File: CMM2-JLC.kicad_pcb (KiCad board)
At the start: 4 copper layers, 130 x 102 mm, 100 parts, among them J1 Nunchuck, J2 VGA, J3 EXTERNAL I/O, J4 USB_C_Receptacle_USB2.0, J5 Audio, J6 USB A Host, J7 SWD, J8 Micro_SD_Card_Det, J9 Boot select, SW1 Reset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

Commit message: VGA DAC gelayoutet
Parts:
- moved C1 329.2 mm to (-74.8, 78.2)
- moved C13 329.2 mm to (-74.8, 76.2)
- moved C14 329.2 mm to (-61.1, 63.9)
- moved C15 329.2 mm to (-95.2, 95.3)
- moved C2 329.2 mm to (-92.3, 94.8)
- moved C4 329.2 mm to (-82.1, 82.5)
- moved C5 329.2 mm to (-102.4, 104.1)
- moved C6 329.2 mm to (-93.6, 83.0)
- moved C7 329.2 mm to (-71.5, 64.2)
- moved C8 329.2 mm to (-83.2, 85.0)
- moved R1 329.2 mm to (-77.8, 78.2)
- moved R3 329.2 mm to (-79.2, 80.2)
- moved R42 329.2 mm to (-86.1, 87.0)
- moved R43 329.2 mm to (-72.0, 68.9)
- moved R46 329.2 mm to (-92.7, 92.8)
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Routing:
- net /RESET: track 0.00 -> 56.4 mm
- net /VGA_RED: track 0.00 -> 9.84 mm
- net /PH1: track 0.00 -> 9.28 mm
- net /PH0: track 0.00 -> 9.24 mm
- net /VGA_BLUE: track 0.00 -> 8.17 mm
- net /PC15: track 0.00 -> 8.03 mm
- net /VGA_GREEN: track 0.00 -> 8.01 mm
- net /PC14: track 0.00 -> 7.94 mm
- net Net-(R32-Pad1): track 0.00 -> 3.04 mm
- net Net-(R25-Pad1): track 0.00 -> 3.02 mm
- net Net-(R13-Pad2): track 0.00 -> 3.02 mm
- net Net-(R26-Pad1): track 0.00 -> 3.02 mm
- net Net-(R20-Pad1): track 0.00 -> 3.02 mm
- net Net-(R19-Pad1): track 0.00 -> 3.02 mm
- net Net-(R14-Pad1): track 0.00 -> 3.02 mm
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
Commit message: VGA Routing
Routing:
- net /PI10: track 0.00 -> 96.6 mm, vias 0 -> 2
- net /PI9: track 0.00 -> 93.0 mm, vias 0 -> 2
- net /PC0: track 0.00 -> 82.2 mm, vias 0 -> 4
- net /PB1: track 0.00 -> 77.7 mm, vias 0 -> 4
- net /PI4: track 0.00 -> 75.8 mm
- net /PG10: track 0.00 -> 75.2 mm, vias 0 -> 2
- net /PI5: track 0.00 -> 72.7 mm
- net /PG11: track 0.00 -> 69.8 mm
- net /PI6: track 0.00 -> 69.6 mm
- net /PI7: track 0.00 -> 68.0 mm
- net /PH10: track 0.00 -> 60.9 mm, vias 0 -> 4
- net /PH9: track 0.00 -> 58.5 mm, vias 0 -> 4
- net /PG6: track 0.00 -> 58.2 mm, vias 0 -> 2
- net /PI2: track 0.00 -> 50.4 mm, vias 0 -> 2
- net /PH13: track 0.00 -> 44.7 mm, vias 0 -> 2
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
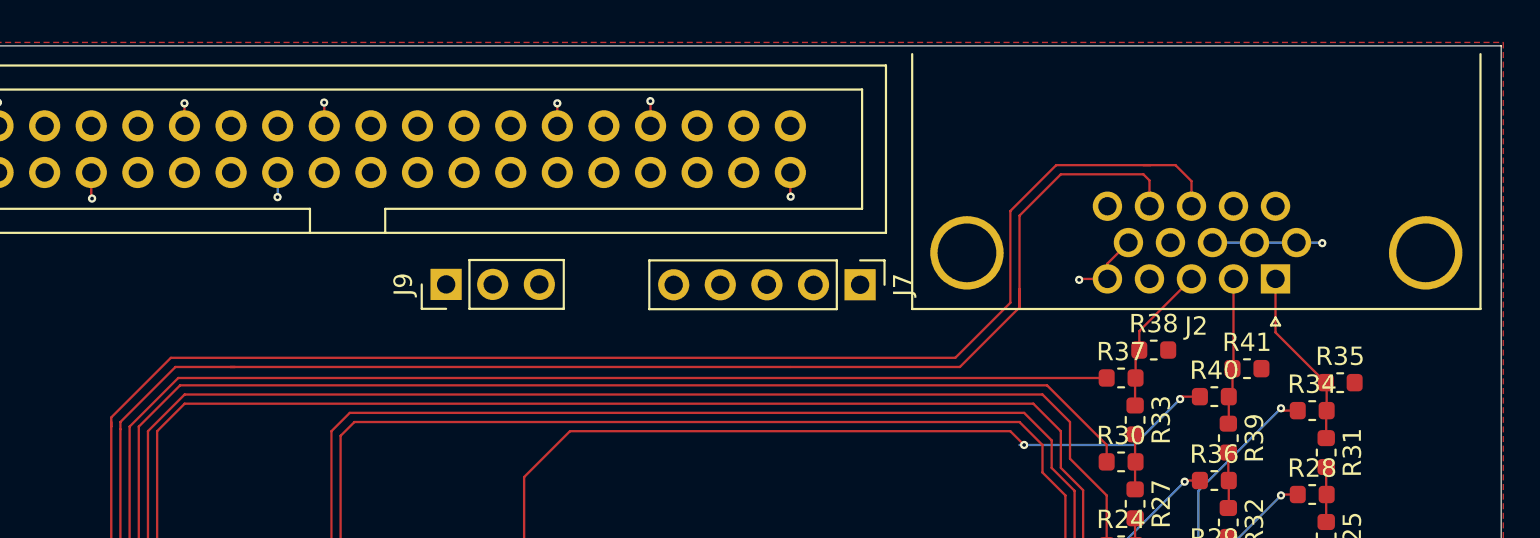
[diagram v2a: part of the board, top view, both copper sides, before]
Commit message: Replace VGA connector
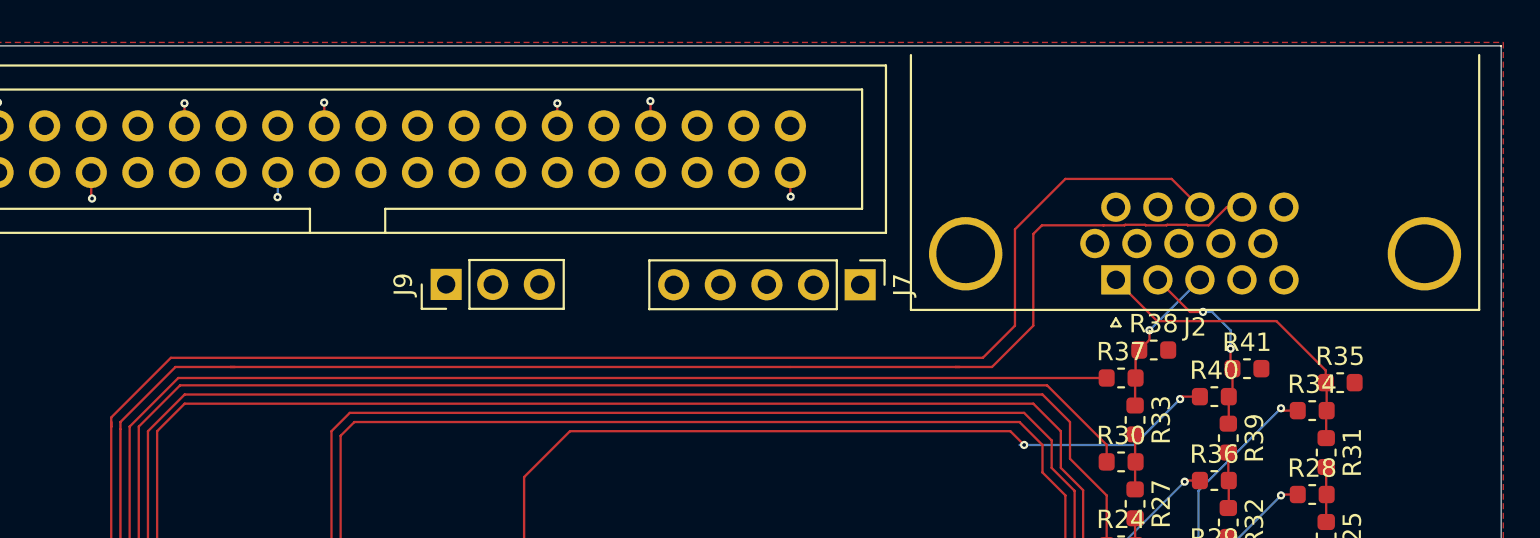
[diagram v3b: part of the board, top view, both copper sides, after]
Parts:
- J2: footprint Connector_Dsub:DSUB-15-HD_Male_Horizontal_P2.29x1.98mm_EdgePinOffset8.35mm_Housed_MountingHolesOffset10.89mm -> Connector_Dsub:DSUB-15-HD_Female_Horizontal_P2.29x1.98mm_EdgePinOffset8.35mm_Housed_MountingHolesOffset10.89mm
- moved J2 8.70 mm to (129.0, 32.8)
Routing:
- net GND: track 92.1 -> 82.1 mm, vias 57 -> 55
- net /VGA_RED: track 9.84 -> 17.2 mm
- net /VGA_GREEN: track 8.01 -> 10.4 mm, vias 0 -> 2
- net /PI9: track 93.0 -> 95.3 mm
- net /PI10: track 96.6 -> 95.4 mm
- net /VGA_BLUE: track 8.17 -> 8.48 mm, vias 0 -> 1

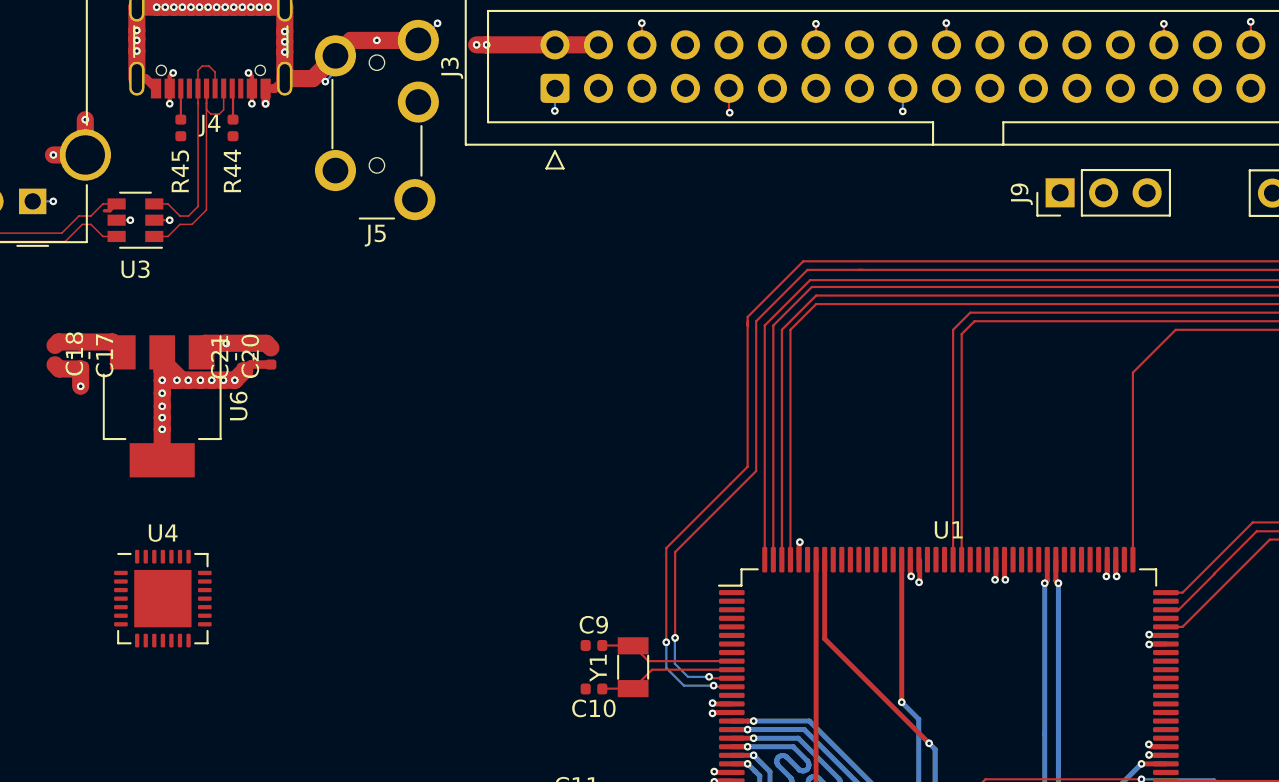
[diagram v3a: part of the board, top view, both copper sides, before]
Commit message: USB Host routed
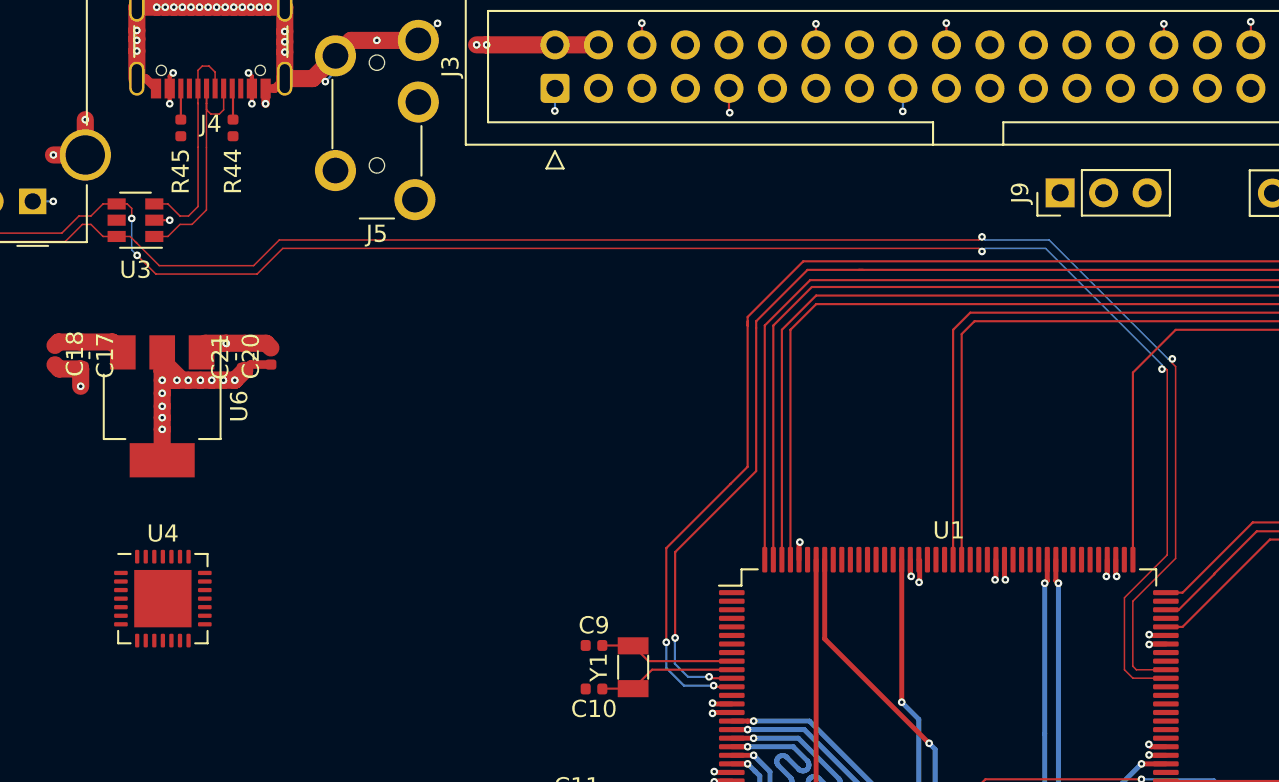
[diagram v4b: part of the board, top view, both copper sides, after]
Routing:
- net /USB_HOST_D-: track 10.5 -> 99.1 mm, vias 0 -> 4
- net /USB_HOST_D+: track 11.1 -> 98.3 mm, vias 0 -> 2
- net +5V: track 17.2 -> 16.4 mm, vias 8 -> 7
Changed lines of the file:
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@@
     (thickness 1.6)
     (drawings 33)
-    (tracks 2975)
+    (tracks 3021)
     (zones 0)
     (modules 100)
@@
   )
   (setup
-    (last_trace_width 0.127)
+    (last_trace_width 0.09)
     (user_trace_width 0.09)
     (user_trace_width 0.127)
@@
   (segment (start 34.0025 41.7125) (end 33.8 41.915) (width 1) (layer F.Cu) (net 146))
   (segment (start 35.3 41.7125) (end 34.0025 41.7125) (width 1) (layer F.Cu) (net 146))
-  (via (at 38.2 34.6) (size 0.45) (drill 0.2) (layers F.Cu B.Cu) (net 146))
-  (segment (start 37.4 34.6) (end 38.2 34.6) (width 0.127) (layer F.Cu) (net 146))
   (via (at 33.7 33.5) (size 0.45) (drill 0.2) (layers F.Cu B.Cu) (net 146))
   (segment (start 32.5 33.5) (end 33.7 33.5) (width 0.127) (layer B.Cu) (net 146))
@@
   (segment (start 42.15 27.780001) (end 42.155 27.785001) (width 0.09) (layer F.Cu) (net 200))
   (segment (start 42.15 26.91) (end 42.15 27.780001) (width 0.09) (layer F.Cu) (net 200))
-  (segment (start 42.155 27.785001) (end 42.155 33.798516) (width 0.09) (layer F.Cu) (net 200))
+  (segment (start 42.155 27.785001) (end 42.155 30.345) (width 0.09) (layer F.Cu) (net 200))
   (segment (start 40.395001 33.65) (end 39.6 33.65) (width 0.09) (layer F.Cu) (net 200))
   (segment (start 41.100001 34.355) (end 40.395001 33.65) (width 0.09) (layer F.Cu) (net 200))
   (segment (start 41.598516 34.355) (end 41.100001 34.355) (width 0.09) (layer F.Cu) (net 200))
   (segment (start 42.155 33.798516) (end 41.598516 34.355) (width 0.09) (layer F.Cu) (net 200))
+  (segment (start 42.155 30.345) (end 42.155 33.798516) (width 0.09) (layer F.Cu) (net 200))
   (segment (start 42.65 28.15) (end 42.65 26.91) (width 0.09) (layer F.Cu) (net 201))
   (segment (start 42.9 28.4) (end 42.65 28.15) (width 0.09) (layer F.Cu) (net 201))
@@
   (segment (start 42.65 26.91) (end 42.65 27.780001) (width 0.09) (layer F.Cu) (net 201))
   (segment (start 42.65 27.780001) (end 42.645 27.785001) (width 0.09) (layer F.Cu) (net 201))
-  (segment (start 42.645 27.785001) (end 42.645 34.001484) (width 0.09) (layer F.Cu) (net 201))
+  (segment (start 42.645 27.785001) (end 42.645 30.355) (width 0.09) (layer F.Cu) (net 201))
   (segment (start 40.395001 35.55) (end 39.6 35.55) (width 0.09) (layer F.Cu) (net 201))
   (segment (start 41.100001 34.845) (end 40.395001 35.55) (width 0.09) (layer F.Cu) (net 201))
   (segment (start 41.801484 34.845) (end 41.100001 34.845) (width 0.09) (layer F.Cu) (net 201))
   (segment (start 42.645 34.001484) (end 41.801484 34.845) (width 0.09) (layer F.Cu) (net 201))
+  (segment (start 42.645 30.355) (end 42.645 34.001484) (width 0.09) (layer F.Cu) (net 201))
   (segment (start 29.653518 35.153518) (end 30.345 35.845) (width 0.09) (layer F.Cu) (net 202))
   (segment (start 28 33.5) (end 29.653518 35.153518) (width 0.09) (layer F.Cu) (net 202))
@@
   (segment (start 34.401484 35.845) (end 30.345 35.845) (width 0.09) (layer F.Cu) (net 202))
   (segment (start 35.401484 34.845) (end 34.401484 35.845) (width 0.09) (layer F.Cu) (net 202))
-  (segment (start 37.002001 34.047999) (end 36.688399 34.047999) (width 0.2) (layer F.Cu) (net 203))
-  (segment (start 37.4 33.65) (end 37.002001 34.047999) (width 0.2) (layer F.Cu) (net 203))
+  (segment (start 98.67 60.855) (end 96.951484 60.855) (width 0.09) (layer F.Cu) (net 202))
+  (segment (start 98.675 60.85) (end 98.67 60.855) (width 0.09) (layer F.Cu) (net 202))
+  (segment (start 96.951484 60.855) (end 96.745 60.648516) (width 0.09) (layer F.Cu) (net 202))
+  (segment (start 96.745 60.648516) (end 96.745 56.851484) (width 0.09) (layer F.Cu) (net 202))
+  (segment (start 96.745 56.851484) (end 99.245 54.351484) (width 0.09) (layer F.Cu) (net 202))
+  (segment (start 99.050521 42.954038) (end 99.050521 42.699479) (width 0.09) (layer F.Cu) (net 202))
+  (segment (start 99.245 54.351484) (end 99.245 43.148517) (width 0.09) (layer F.Cu) (net 202))
+  (segment (start 99.245 43.148517) (end 99.050521 42.954038) (width 0.09) (layer F.Cu) (net 202))
+  (via (at 99.050521 42.699479) (size 0.45) (drill 0.2) (layers F.Cu B.Cu) (net 202))
+  (segment (start 88.116549 35.755) (end 87.936549 35.575) (width 0.09) (layer B.Cu) (net 202))
+  (segment (start 99.050521 42.699479) (end 98.795962 42.699479) (width 0.09) (layer B.Cu) (net 202))
+  (segment (start 98.795962 42.699479) (end 91.851483 35.755) (width 0.09) (layer B.Cu) (net 202))
+  (segment (start 91.851483 35.755) (end 88.116549 35.755) (width 0.09) (layer B.Cu) (net 202))
+  (via (at 87.936549 35.575) (size 0.45) (drill 0.2) (layers F.Cu B.Cu) (net 202))
+  (segment (start 87.756549 35.755) (end 46.898516 35.755) (width 0.09) (layer F.Cu) (net 202))
+  (segment (start 87.936549 35.575) (end 87.756549 35.755) (width 0.09) (layer F.Cu) (net 202))
+  (segment (start 46.898516 35.755) (end 45.398516 37.255) (width 0.09) (layer F.Cu) (net 202))
+  (segment (start 45.398516 37.255) (end 39.893178 37.255) (width 0.09) (layer F.Cu) (net 202))
+  (segment (start 38.188178 35.55) (end 38.569089 35.930911) (width 0.09) (layer F.Cu) (net 202))
+  (segment (start 37.4 35.55) (end 38.188178 35.55) (width 0.09) (layer F.Cu) (net 202))
+  (segment (start 38.569089 35.930911) (end 38.491662 35.853484) (width 0.09) (layer F.Cu) (net 202))
+  (segment (start 39.893178 37.255) (end 38.569089 35.930911) (width 0.09) (layer F.Cu) (net 202))
   (segment (start 30 34.807035) (end 30.547965 35.355) (width 0.09) (layer F.Cu) (net 203))
   (segment (start 30 33.5) (end 30 34.807035) (width 0.09) (layer F.Cu) (net 203))
@@
   (segment (start 35.198516 34.355) (end 34.198516 35.355) (width 0.09) (layer F.Cu) (net 203))
   (segment (start 34.198516 35.355) (end 30.547965 35.355) (width 0.09) (layer F.Cu) (net 203))
+  (segment (start 98.67 61.345) (end 96.748516 61.345) (width 0.09) (layer F.Cu) (net 203))
+  (segment (start 98.675 61.35) (end 98.67 61.345) (width 0.09) (layer F.Cu) (net 203))
+  (segment (start 96.748516 61.345) (end 96.255 60.851484) (width 0.09) (layer F.Cu) (net 203))
+  (segment (start 96.255 60.851484) (end 96.255 56.648516) (width 0.09) (layer F.Cu) (net 203))
+  (segment (start 96.255 56.648516) (end 98.755 54.148516) (width 0.09) (layer F.Cu) (net 203))
+  (segment (start 98.704038 43.300521) (end 98.449479 43.300521) (width 0.09) (layer F.Cu) (net 203))
+  (segment (start 98.755 54.148516) (end 98.755 43.351483) (width 0.09) (layer F.Cu) (net 203))
+  (segment (start 98.755 43.351483) (end 98.704038 43.300521) (width 0.09) (layer F.Cu) (net 203))
+  (via (at 98.449479 43.300521) (size 0.45) (drill 0.2) (layers F.Cu B.Cu) (net 203))
+  (segment (start 88.116549 36.245) (end 87.936549 36.425) (width 0.09) (layer B.Cu) (net 203))
+  (segment (start 91.648517 36.245) (end 88.116549 36.245) (width 0.09) (layer B.Cu) (net 203))
+  (segment (start 98.449479 43.045962) (end 91.648517 36.245) (width 0.09) (layer B.Cu) (net 203))
+  (segment (start 98.449479 43.300521) (end 98.449479 43.045962) (width 0.09) (layer B.Cu) (net 203))
+  (via (at 87.936549 36.425) (size 0.45) (drill 0.2) (layers F.Cu B.Cu) (net 203))
+  (segment (start 87.756549 36.245) (end 47.101484 36.245) (width 0.09) (layer F.Cu) (net 203))
+  (segment (start 87.936549 36.425) (end 87.756549 36.245) (width 0.09) (layer F.Cu) (net 203))
+  (segment (start 47.101484 36.245) (end 45.601484 37.745) (width 0.09) (layer F.Cu) (net 203))
+  (segment (start 45.601484 37.745) (end 39.69021 37.745) (width 0.09) (layer F.Cu) (net 203))
+  (via (at 38.282002 34.5) (size 0.45) (drill 0.2) (layers F.Cu B.Cu) (net 203))
+  (segment (start 38.282002 33.912002) (end 38.282002 34.5) (width 0.09) (layer F.Cu) (net 203))
+  (segment (start 38.02 33.65) (end 38.282002 33.912002) (width 0.09) (layer F.Cu) (net 203))
+  (segment (start 37.4 33.65) (end 38.02 33.65) (width 0.09) (layer F.Cu) (net 203))
+  (via (at 38.597605 36.652395) (size 0.45) (drill 0.2) (layers F.Cu B.Cu) (net 203))
+  (segment (start 38.282002 36.336792) (end 38.597605 36.652395) (width 0.09) (layer B.Cu) (net 203))
+  (segment (start 38.282002 34.5) (end 38.282002 36.336792) (width 0.09) (layer B.Cu) (net 203))
+  (segment (start 39.69021 37.745) (end 38.597605 36.652395) (width 0.09) (layer F.Cu) (net 203))
   (zone (net 1) (net_name GND) (layer GND) (hatch edge 0.508)
     (connect_pads yes (clearance 0.127))

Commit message: Add decoupling, start routing of 40pin extension header
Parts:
- removed TP-3V3, TP-5V1, TP-GND1: TestPoint, TestPoint:TestPoint_Pad_2.0x2.0mm
- added C24: 100n, Capacitor_SMD:C_0402_1005Metric, F.Cu at (89.0, 52.7)
- added C25: 100n, Capacitor_SMD:C_0402_1005Metric, F.Cu at (71.6, 63.1)
- added C26: 100n, Capacitor_SMD:C_0402_1005Metric, F.Cu at (100.5, 59.1)
- added C27: 100n, Capacitor_SMD:C_0402_1005Metric, F.Cu at (71.3, 74.1)
- added C28: 100n, Capacitor_SMD:C_0402_1005Metric, F.Cu at (83.3, 81.6)
- added C29: 100n, Capacitor_SMD:C_0402_1005Metric, F.Cu at (101.1, 65.6)
- added C30: 100n, Capacitor_SMD:C_0402_1005Metric, F.Cu at (77.3, 81.7)
- added C31: 100n, Capacitor_SMD:C_0402_1005Metric, B.Cu at (88.5, 77.8)
- added C32: 100n, Capacitor_SMD:C_0402_1005Metric, F.Cu at (84.0, 52.7)
- added C33: 100n, Capacitor_SMD:C_0402_1005Metric, F.Cu at (100.6, 78.7)
- added C34: 100n, Capacitor_SMD:C_0402_1005Metric, F.Cu at (77.8, 52.7)
- added C35: 100n, Capacitor_SMD:C_0402_1005Metric, F.Cu at (100.2, 72.0)
- added C36: 100n, Capacitor_SMD:C_0402_1005Metric, F.Cu at (71.6, 67.2)
- added C37: 100n, Capacitor_SMD:C_0402_1005Metric, F.Cu at (95.5, 52.7)
- C22, C23, C4, C5: moved to B.Cu
- moved C6 192.3 mm to (98.7, 80.1), turned to 45 degrees
- moved C5 191.4 mm to (88.2, 86.8), turned to 180 degrees
- moved C2 186.0 mm to (93.6, 101.8)
- moved C4 176.3 mm to (94.1, 89.9), turned to 180 degrees
- moved C7 173.5 mm to (102.0, 59.7), turned to 270 degrees
- moved C1 165.2 mm to (88.7, 101.8)
- moved C22 151.4 mm to (80.8, 89.9), turned to 180 degrees
- moved C23 118.8 mm to (77.3, 89.9)
- moved C3 114.1 mm to (73.9, 94.9), turned to 270 degrees
- moved J9 102.8 mm to (190.0, 65.7)
- moved J7 94.4 mm to (200.1, 74.0)
- moved U4 14.5 mm to (47.9, 44.5)
- moved C20 11.5 mm to (34.9, 42.5)
- moved C21 11.5 mm to (33.4, 42.6)
- moved U6 11.5 mm to (28.6, 45.5)
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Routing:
- net /PB12: track 0.00 -> 115.0 mm, vias 0 -> 5
- net /PE2: track 0.00 -> 109.8 mm, vias 0 -> 3
- net /NUNCHUCK_SDA: track 0.00 -> 103.4 mm, vias 0 -> 7
- net /PA6: track 0.00 -> 91.2 mm, vias 0 -> 5
- net /PA3: track 0.00 -> 88.6 mm, vias 0 -> 1
- net /PA2: track 0.00 -> 81.5 mm, vias 0 -> 1
- net /PC1: track 0.00 -> 80.2 mm, vias 0 -> 1
- net /PI11: track 0.00 -> 77.5 mm, vias 0 -> 2
- net /PB14: track 0.00 -> 76.9 mm, vias 0 -> 1
- net /PB13: track 0.00 -> 73.3 mm, vias 0 -> 1
- net GND: track 82.1 -> 155.3 mm, vias 55 -> 561
- net /PA5: track 0.00 -> 72.4 mm, vias 0 -> 4
- net /PB15: track 0.00 -> 71.0 mm, vias 0 -> 2
- net /NUNCHUCK_SCL: track 0.00 -> 70.0 mm, vias 0 -> 2
- net /PA4: track 0.00 -> 69.0 mm, vias 0 -> 3
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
